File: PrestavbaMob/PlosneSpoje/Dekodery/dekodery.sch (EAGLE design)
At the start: 3 parts, among them IC1 ATMEGA48/88/168-AU

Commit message: Prvni verze desky pro dekodery.
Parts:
- added C1, C2, C3: (no value), #PaJa_30:C-KERAMIK_SMD_1206
- added CON1: MLW06_90°, #PaJa_konektory:MLW06_90°
- added D1, D2, D3, D4, D5, D6: LED_SMD_1206, #PaJa_30:LED_SMD_1206
- added K3, K5: (no value), #PaJa_konektory:PSH02-02W
- added K4: (no value), #PaJa_konektory:PSH02-03W
- added Q2: Q_HC-49U_SMD, #PaJa_30:Q_HC-49U_SMD
- added R1, R10, R2, R3, R4, R5, R6, R7, R8, R9: (no value), #PaJa_30:R_SMD_1206
- added T1, T2: BUZ11, ondrap:BUZ11
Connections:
- new net N$10: D1.A, IC1.PD5(T1/OC0B/PCINT21)
- new net N$11: D2.A, IC1.PD6(AIN0/OC0A/PCINT22)
- new net N$12: D3.A, IC1.PD7(AIN1/PCINT23)
- new net N$13: D4.A, IC1.PB0(ICP1/CLKO/PCINT0)
- new net N$14: D5.A, IC1.PB1(OC1A/PCINT1)
- new net N$15: D6.A, IC1.PB2(SS/OC1B/PCINT2)
- new net N$16: D1.K, R1.1
- new net N$17: D2.K, R2.1
- new net N$18: D3.K, R3.1
- new net N$19: D4.K, R4.1
- new net N$20: D5.K, R5.1
- new net N$21: D6.K, R6.1
- new net N$22: C2.2, IC1.PB6(XTAL1/TOSC1/PCINT6), Q2.1
- new net N$23: IC1.PC4(ADC4/SDA/PCINT12), K5.2, R8.1, T2.D
- new net N$24: K4.3, R10.1, R9.2, T1.G, T2.G
- new net N$26: K4.2, R10.2, T2.S
- new net N$27: K4.1, R9.1, T1.S
- new net N$5: IC1.PC5(ADC5/SCL/PCINT13), K5.1, R7.2, T1.D
- new net N$6: C3.2, IC1.PB7(XTAL2/TOSC2/PCINT7), Q2.2
- new net N$7: CON1.1, IC1.PB4(MISO/PCINT4)
- new net N$8: CON1.3, IC1.PB5(SCK/PCINT5)
- new net N$9: CON1.4, IC1.PB3(MOSI/OC2A/PCINT3)
- new net RST: CON1.5, IC1.PC6(/RESET/PCINT14)
- net GND: now also C1.1, C2.1, C3.1, CON1.6, IC1.AGND, IC1.GND@2, K3.2, R1.2, R2.2, R3.2, R4.2, R5.2, R6.2
- net N$1: now also K2.2; no longer K2.1
- net N$2: now also K2.1; no longer K2.2
- net N$3: now also K1.2; no longer K1.1
- net N$4: now also K1.1; no longer K1.2
- net VCC: now also C1.2, CON1.2, IC1.VCC@2, K3.1, R7.1, R8.2
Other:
- moved on the sheet: K1, K2

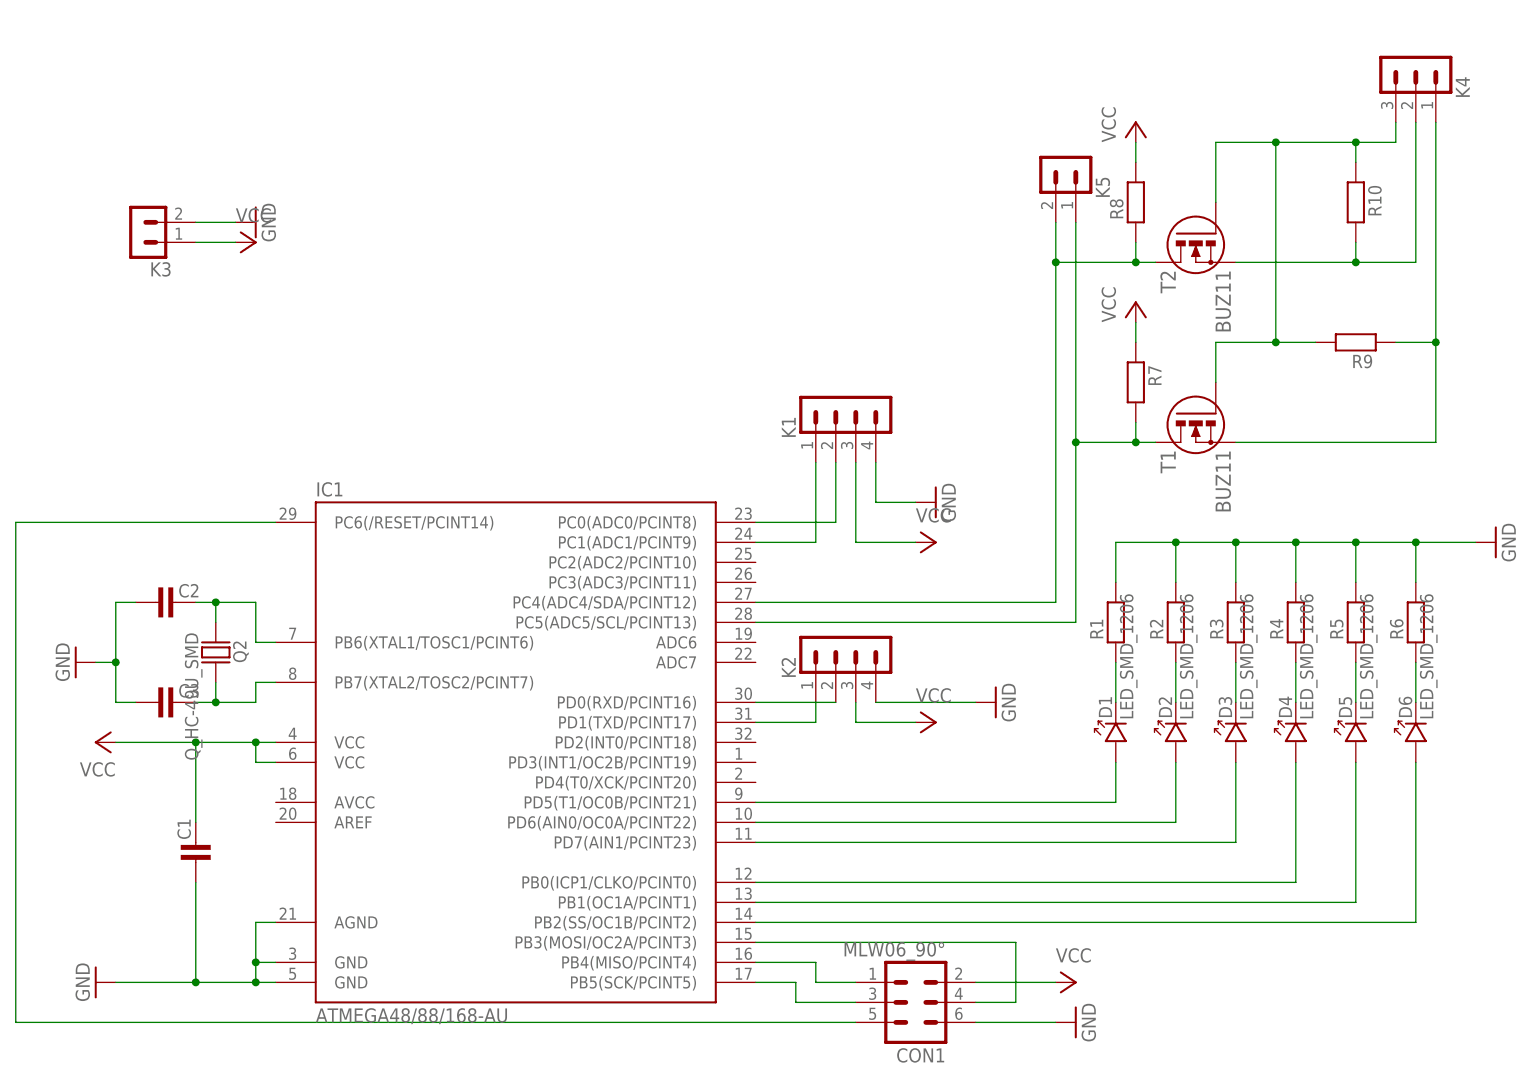
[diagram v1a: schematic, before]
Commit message: Pridan pull-up rezistor k resetu a zapojeni avcc.
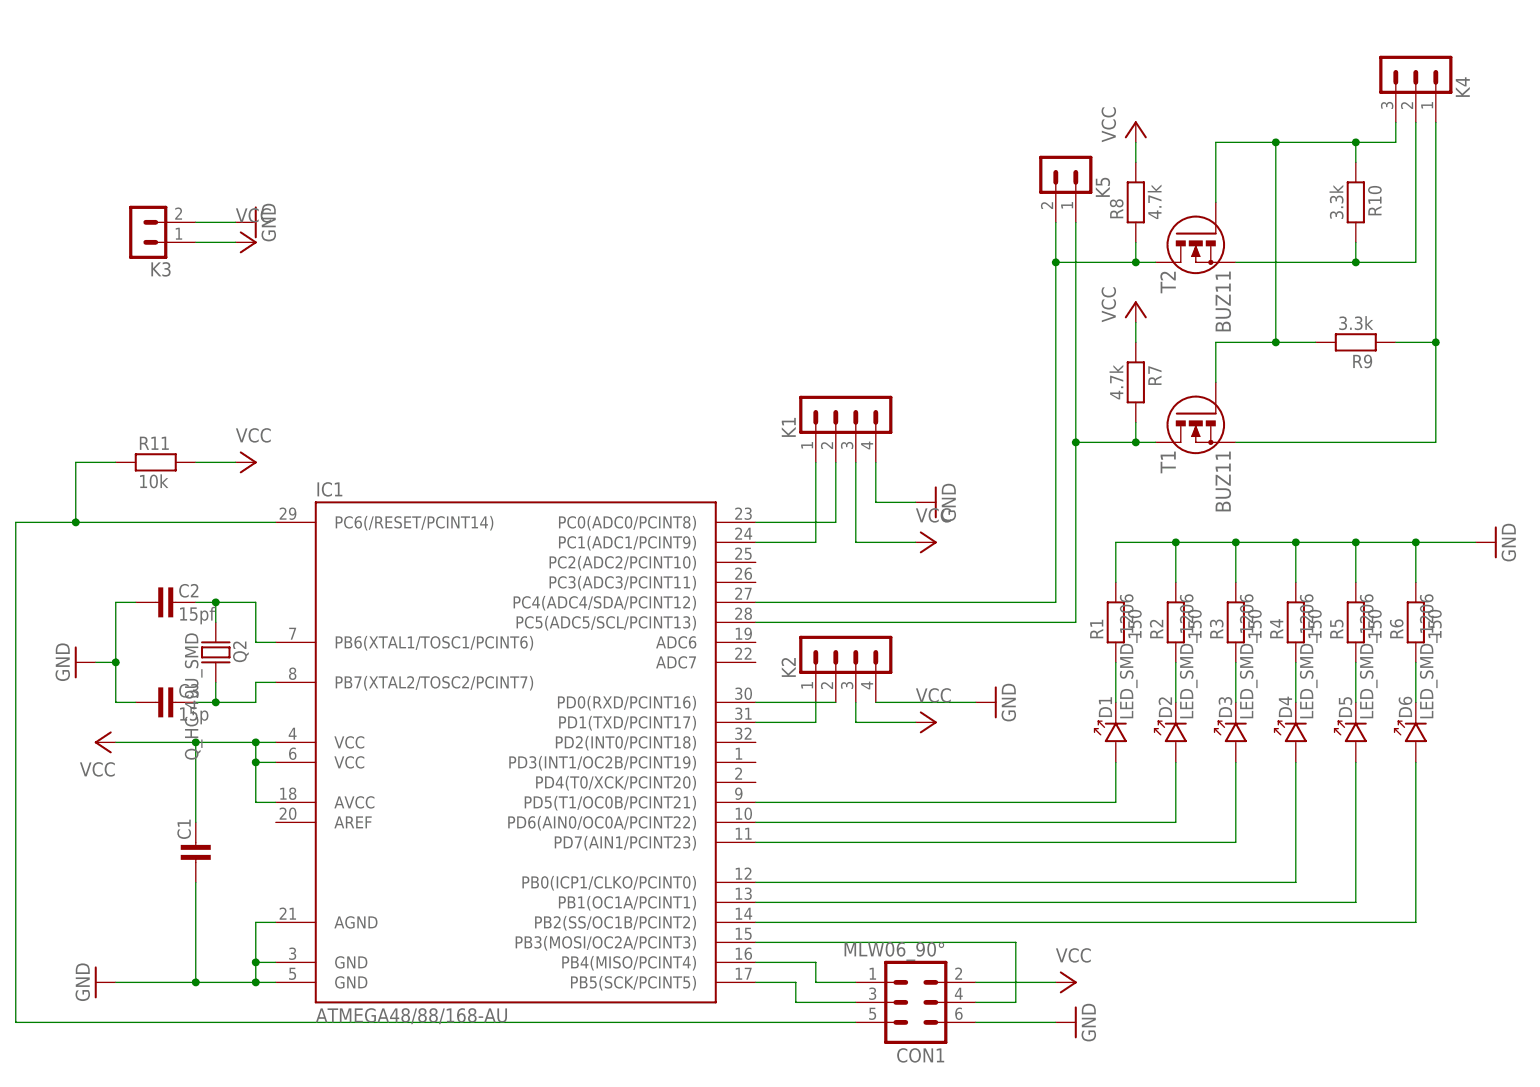
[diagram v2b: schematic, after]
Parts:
- added R11: 10k, #PaJa_30:R_SMD_1206
- C2: value (none) -> 15pf
- C3: value (none) -> 15p
- R1, R2, R3, R4, R5, R6: value (none) -> 150
- R10, R9: value (none) -> 3.3k
- R7, R8: value (none) -> 4.7k
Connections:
- net RST: now also R11.1
- net VCC: now also IC1.AVCC, R11.2
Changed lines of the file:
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@@
 <part name="P+3" library="supply1" deviceset="VCC" device=""/>
 <part name="C1" library="#PaJa_30" deviceset="C-KERAMIK" device="_SMD_1206"/>
-<part name="C2" library="#PaJa_30" deviceset="C-KERAMIK" device="_SMD_1206"/>
-<part name="C3" library="#PaJa_30" deviceset="C-KERAMIK" device="_SMD_1206"/>
+<part name="C2" library="#PaJa_30" deviceset="C-KERAMIK" device="_SMD_1206" value="15pf"/>
+<part name="C3" library="#PaJa_30" deviceset="C-KERAMIK" device="_SMD_1206" value="15p"/>
 <part name="GND4" library="supply1" deviceset="GND" device=""/>
 <part name="CON1" library="#PaJa_konektory" deviceset="MLW06" device="_90°"/>
@@
 <part name="D5" library="#PaJa_30" deviceset="LED" device="_SMD_1206"/>
 <part name="D6" library="#PaJa_30" deviceset="LED" device="_SMD_1206"/>
-<part name="R1" library="#PaJa_30" deviceset="R" device="_SMD_1206"/>
-<part name="R2" library="#PaJa_30" deviceset="R" device="_SMD_1206"/>
-<part name="R3" library="#PaJa_30" deviceset="R" device="_SMD_1206"/>
-<part name="R4" library="#PaJa_30" deviceset="R" device="_SMD_1206"/>
-<part name="R5" library="#PaJa_30" deviceset="R" device="_SMD_1206"/>
-<part name="R6" library="#PaJa_30" deviceset="R" device="_SMD_1206"/>
+<part name="R1" library="#PaJa_30" deviceset="R" device="_SMD_1206" value="150"/>
+<part name="R2" library="#PaJa_30" deviceset="R" device="_SMD_1206" value="150"/>
+<part name="R3" library="#PaJa_30" deviceset="R" device="_SMD_1206" value="150"/>
+<part name="R4" library="#PaJa_30" deviceset="R" device="_SMD_1206" value="150"/>
+<part name="R5" library="#PaJa_30" deviceset="R" device="_SMD_1206" value="150"/>
+<part name="R6" library="#PaJa_30" deviceset="R" device="_SMD_1206" value="150"/>
 <part name="GND6" library="supply1" deviceset="GND" device=""/>
 <part name="K3" library="#PaJa_konektory" deviceset="PSH02-02" device="W"/>
@@
 <part name="K4" library="#PaJa_konektory" deviceset="PSH02-03" device="W"/>
 <part name="P+6" library="supply1" deviceset="VCC" device=""/>
-<part name="R7" library="#PaJa_30" deviceset="R" device="_SMD_1206"/>
-<part name="R8" library="#PaJa_30" deviceset="R" device="_SMD_1206"/>
+<part name="R7" library="#PaJa_30" deviceset="R" device="_SMD_1206" value="4.7k"/>
+<part name="R8" library="#PaJa_30" deviceset="R" device="_SMD_1206" value="4.7k"/>
 <part name="P+7" library="supply1" deviceset="VCC" device=""/>
-<part name="R9" library="#PaJa_30" deviceset="R" device="_SMD_1206"/>
-<part name="R10" library="#PaJa_30" deviceset="R" device="_SMD_1206"/>
+<part name="R9" library="#PaJa_30" deviceset="R" device="_SMD_1206" value="3.3k"/>
+<part name="R10" library="#PaJa_30" deviceset="R" device="_SMD_1206" value="3.3k"/>
 <part name="K5" library="#PaJa_konektory" deviceset="PSH02-02" device="W"/>
+<part name="R11" library="#PaJa_30" deviceset="R" device="_SMD_1206" value="10k"/>
+<part name="P+8" library="supply1" deviceset="VCC" device=""/>
 </parts>
 <sheets>
@@
 <instance part="R10" gate="R" x="200.66" y="134.62" rot="R270"/>
 <instance part="K5" gate="KON" x="165.1" y="134.62" rot="MR0"/>
+<instance part="R11" gate="R" x="48.26" y="101.6"/>
+<instance part="P+8" gate="VCC" x="60.96" y="101.6" rot="R270"/>
 </instances>
 <busses>
@@
 <wire x1="60.96" y1="63.5" x2="60.96" y2="66.04" width="0.1524" layer="91"/>
 <junction x="60.96" y="66.04"/>
+<pinref part="IC1" gate="1" pin="AVCC"/>
+<wire x1="63.5" y1="58.42" x2="60.96" y2="58.42" width="0.1524" layer="91"/>
+<wire x1="60.96" y1="58.42" x2="60.96" y2="63.5" width="0.1524" layer="91"/>
+<junction x="60.96" y="63.5"/>
 </segment>
 <segment>
@@
 <pinref part="P+7" gate="VCC" pin="VCC"/>
 <wire x1="172.72" y1="139.7" x2="172.72" y2="142.24" width="0.1524" layer="91"/>
+</segment>
+<segment>
+<pinref part="P+8" gate="VCC" pin="VCC"/>
+<pinref part="R11" gate="R" pin="2"/>
+<wire x1="58.42" y1="101.6" x2="53.34" y2="101.6" width="0.1524" layer="91"/>
 </segment>
 </net>
@@
 <segment>
 <pinref part="IC1" gate="1" pin="PC6(/RESET/PCINT14)"/>
-<wire x1="63.5" y1="93.98" x2="30.48" y2="93.98" width="0.1524" layer="91"/>
+<wire x1="63.5" y1="93.98" x2="38.1" y2="93.98" width="0.1524" layer="91"/>
+<wire x1="38.1" y1="93.98" x2="30.48" y2="93.98" width="0.1524" layer="91"/>
 <wire x1="30.48" y1="93.98" x2="30.48" y2="30.48" width="0.1524" layer="91"/>
 <pinref part="CON1" gate="C" pin="5"/>
 <wire x1="30.48" y1="30.48" x2="137.16" y2="30.48" width="0.1524" layer="91"/>
-</segment>
-</net>
+<wire x1="38.1" y1="93.98" x2="38.1" y2="101.6" width="0.1524" layer="91"/>
+<junction x="38.1" y="93.98"/>
+<pinref part="R11" gate="R" pin="1"/>
+<wire x1="38.1" y1="101.6" x2="43.18" y2="101.6" width="0.1524" layer="91"/>
+</segment>
+</net>

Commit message: Upravena deska pro dekodery. Rozpracovano zapojeni soucastek a jejich propojeni na desce.
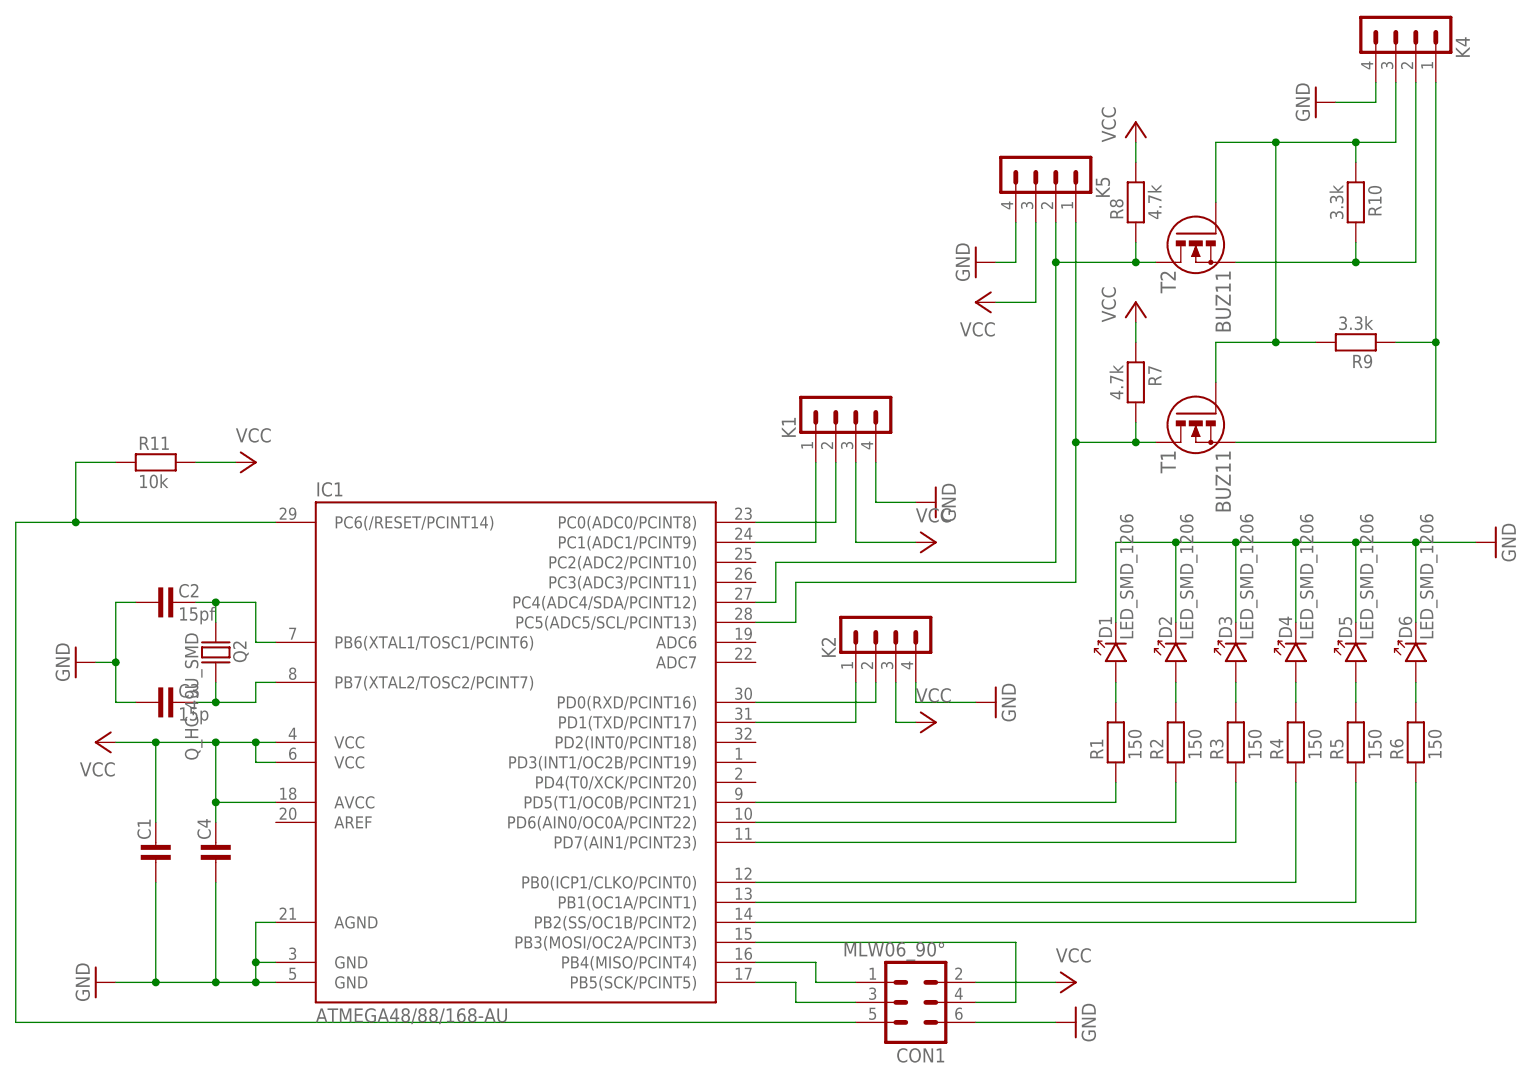
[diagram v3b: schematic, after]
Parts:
- removed K3: (no value), #PaJa_konektory:PSH02-02W
- added C4: (no value), #PaJa_30:C-KERAMIK_SMD_1206
- K4: device #PaJa_konektory:PSH02-03W -> #PaJa_konektory:PSH02-04W
- K5: device #PaJa_konektory:PSH02-02W -> #PaJa_konektory:PSH02-04W
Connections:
- net GND: now also C4.1, D1.K, D2.K, D3.K, D4.K, D5.K, D6.K, K4.4, K5.4; no longer K3.2, R1.2, R2.2, R3.2, R4.2, R5.2, R6.2
- net N$10: now also R1.1; no longer D1.A
- net N$11: now also R2.1; no longer D2.A
- net N$12: now also R3.1; no longer D3.A
- net N$13: now also R4.1; no longer D4.A
- net N$14: now also R5.1; no longer D5.A
- net N$15: now also R6.1; no longer D6.A
- net N$16: now also D1.A, R1.2; no longer D1.K, R1.1
- net N$17: now also D6.A, R6.2; no longer D2.K, R2.1
- net N$18: now also D5.A, R5.2; no longer D3.K, R3.1
- net N$19: now also D4.A, R4.2; no longer D4.K, R4.1
- net N$20: now also D3.A, R3.2; no longer D5.K, R5.1
- net N$21: now also D2.A, R2.2; no longer D6.K, R6.1
- net VCC: now also C4.2, K5.3; no longer K3.1
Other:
- moved on the sheet: C1, D1, D2, D3, D4, D5, D6, K2, R1, R2, R3, R4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

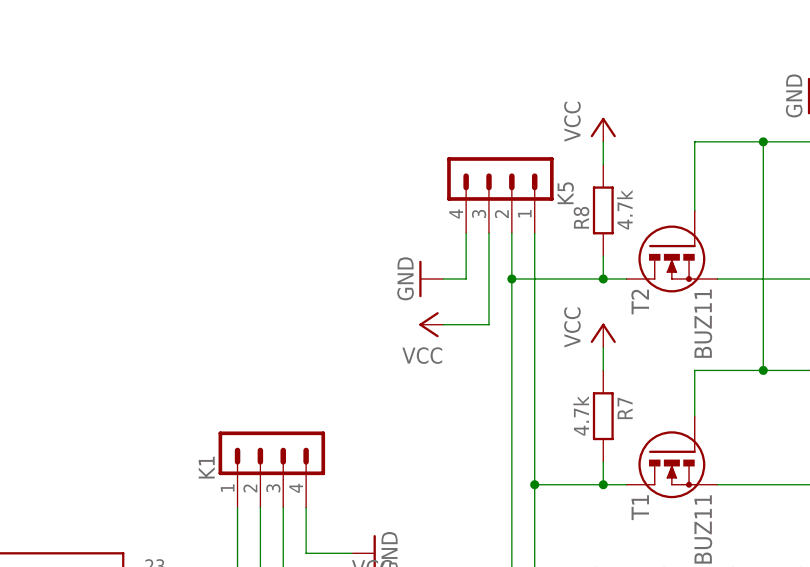
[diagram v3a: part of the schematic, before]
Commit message: Druha verze navrhu desky s propojenim vsech soucastek.
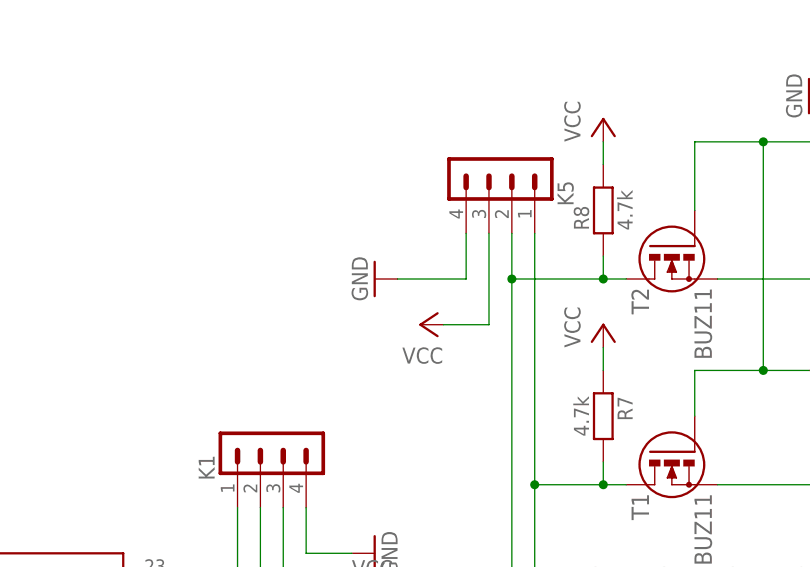
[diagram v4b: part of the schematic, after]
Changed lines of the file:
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@@
 <instance part="P+8" gate="VCC" x="60.96" y="101.6" rot="R270"/>
 <instance part="P+9" gate="VCC" x="152.4" y="121.92" rot="R90"/>
-<instance part="GND8" gate="1" x="152.4" y="127" rot="R270"/>
+<instance part="GND8" gate="1" x="147.32" y="127" rot="R270"/>
 <instance part="GND9" gate="1" x="195.58" y="147.32" rot="R270"/>
 <instance part="C4" gate="C" x="55.88" y="53.34" rot="R90"/>
@@
 <pinref part="GND8" gate="1" pin="GND"/>
 <wire x1="157.48" y1="132.08" x2="157.48" y2="127" width="0.1524" layer="91"/>
-<wire x1="157.48" y1="127" x2="154.94" y2="127" width="0.1524" layer="91"/>
+<wire x1="157.48" y1="127" x2="149.86" y2="127" width="0.1524" layer="91"/>
 </segment>
 </net>
